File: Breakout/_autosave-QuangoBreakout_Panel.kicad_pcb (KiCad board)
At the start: 2 copper layers, 20.3 x 128.5 mm, 23 parts

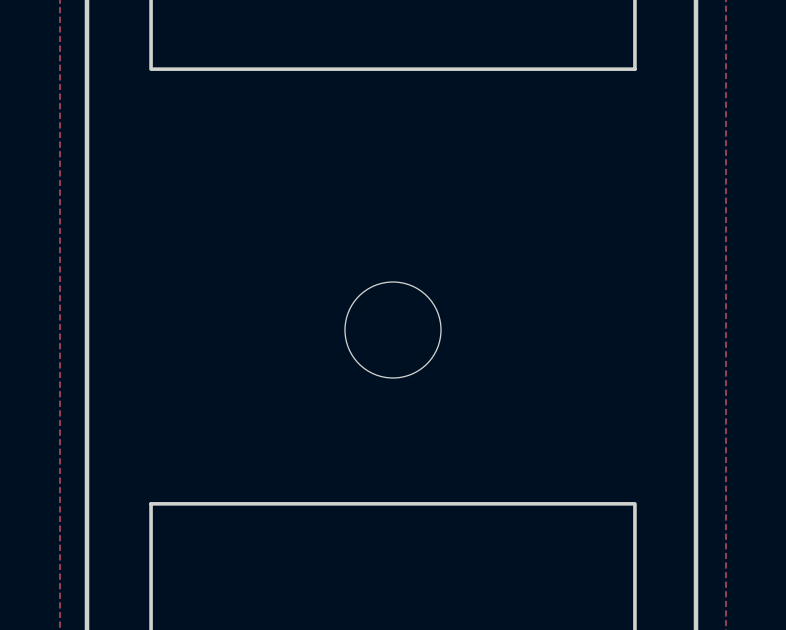
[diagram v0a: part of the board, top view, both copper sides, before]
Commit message: Laid out breakout panel
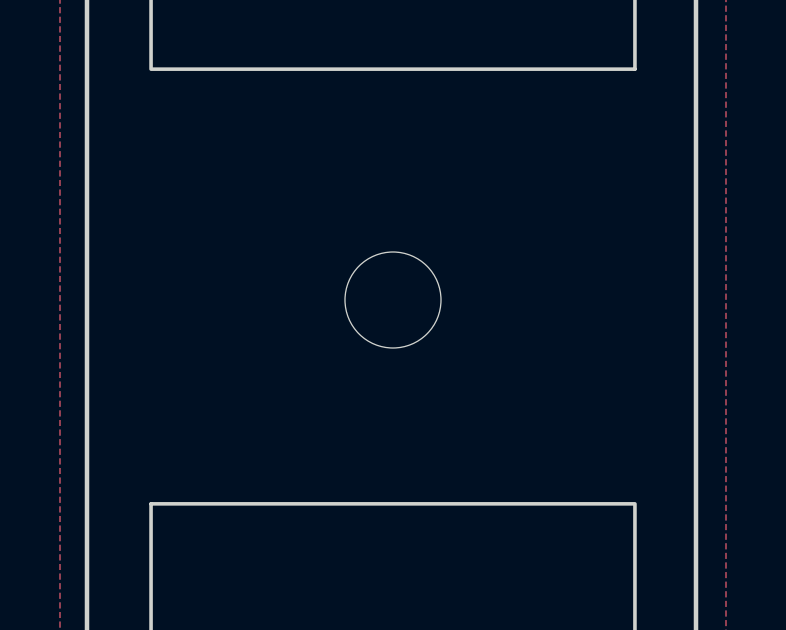
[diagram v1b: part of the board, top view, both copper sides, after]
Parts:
- removed kibuzzard-6498108F: G***, kibuzzard-6498108F
- removed kibuzzard-649810A1: G***, kibuzzard-649810A1
- removed kibuzzard-649810AB: G***, kibuzzard-649810AB
- removed kibuzzard-64981165 (x2): G***, kibuzzard-64981165
- removed kibuzzard-6498118B (x2): G***, kibuzzard-6498118B
- removed kibuzzard-64985DE2: G***, kibuzzard-64985DE2
- removed kibuzzard-64985E01: G***, kibuzzard-64985E01
- added kibuzzard-649866B8: G***, kibuzzard-649866B8, F.Cu at (59.4, 162.1)
- added kibuzzard-649866DB: G***, kibuzzard-649866DB, F.Cu at (54.7, 134.5)
- added kibuzzard-649866EF: G***, kibuzzard-649866EF, F.Cu at (64.1, 134.5)
- added kibuzzard-649869A1: G***, kibuzzard-649869A1, F.Cu at (52.8, 87.9)
- added kibuzzard-649869D7: G***, kibuzzard-649869D7, F.Cu at (65.9, 91.4)
- moved H1 1.00 mm to (59.4, 90.9)
- moved kibuzzard-64985CD8 0.10 mm to (53.5, 112.7)
- moved kibuzzard-64985CE4 0.10 mm to (65.5, 114.0)
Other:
- board text added: "Mountjoy Modular"
- board text added: "Quango Breakout"
- board text added: "Quango Breakout Panel 2023"
- board text removed: "Breakout"
- board text removed: "Mountjoy"
